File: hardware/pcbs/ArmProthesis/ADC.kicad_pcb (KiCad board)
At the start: 4 copper layers, 60.3 x 44.8 mm, 25 parts, among them J2 H_16_2.54mm, SW1 SW_Reed_SPDT, SW2 SW_Reed_SPDT, SW3 SW_Reed_SPDT, SW4 SW_Reed_SPDT, U1 AD7606BSTZ

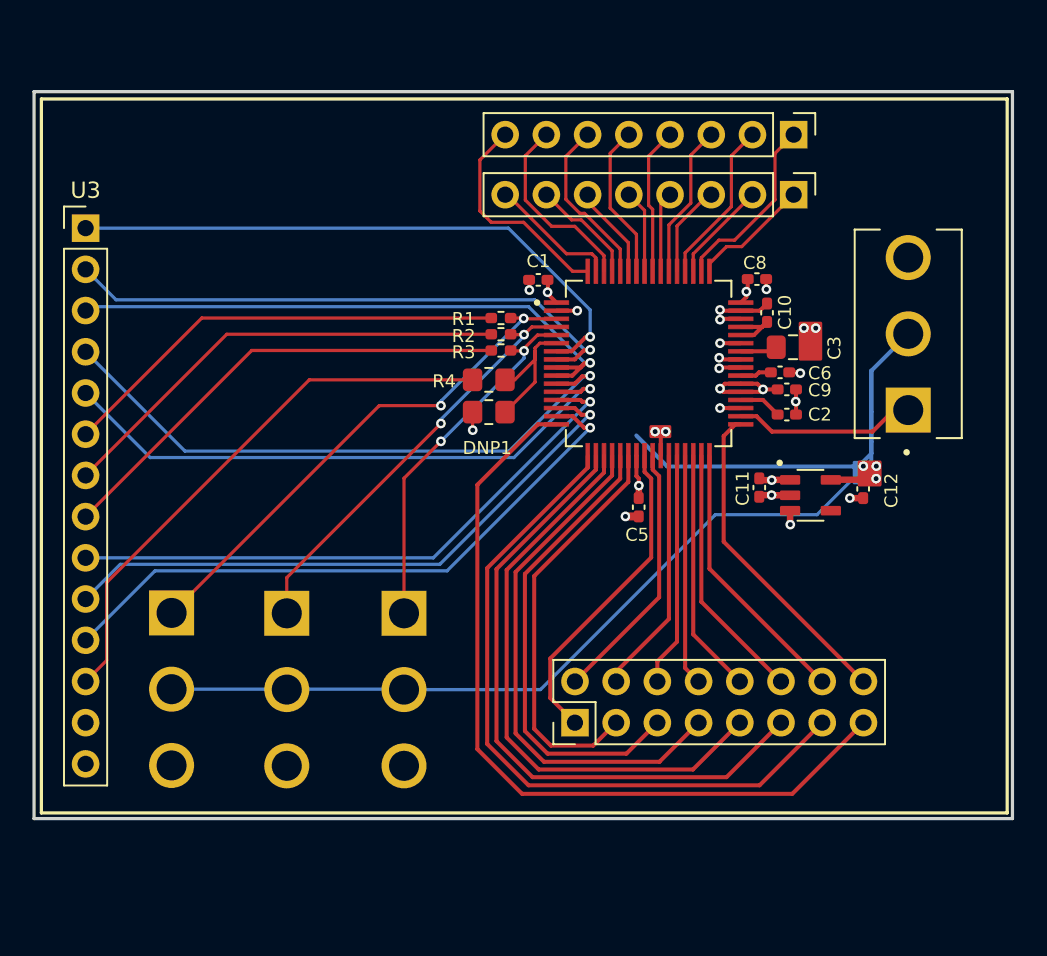
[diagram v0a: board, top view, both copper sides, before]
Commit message: ADC + sEMG changes
sEMG - connector updates
ADC - major changes - connectors, layout changes
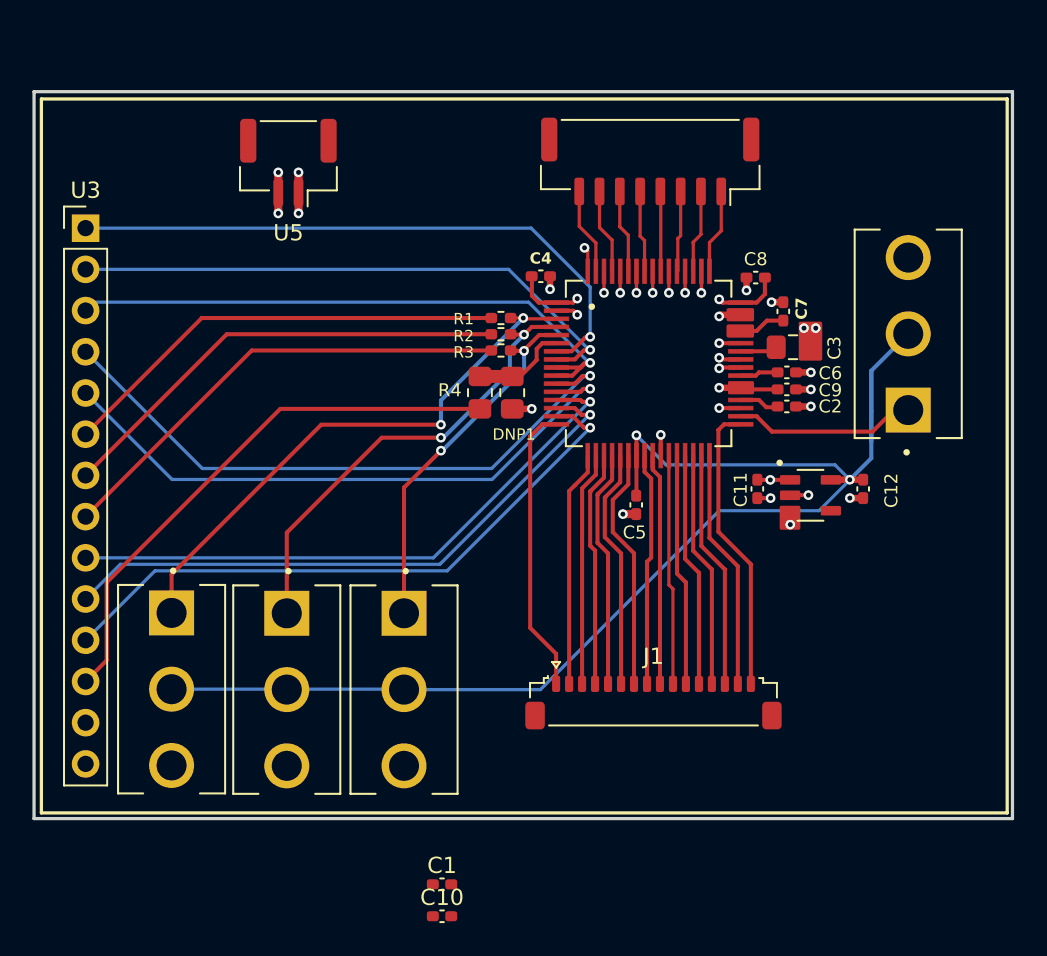
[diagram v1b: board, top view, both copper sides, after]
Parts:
- removed J2: H_16_2.54mm, Connector_PinHeader_2.54mm:PinHeader_2x08_P2.54mm_Vertical
- removed U4: ~, Connector_PinHeader_2.54mm:PinHeader_1x08_P2.54mm_Vertical
- added C4: 0.1uF, Capacitor_SMD:C_0402_1005Metric_Pad0.74x0.62mm_HandSolder, F.Cu at (170.3, 79.5)
- added C7: 1uF, Capacitor_SMD:C_0402_1005Metric_Pad0.74x0.62mm_HandSolder, F.Cu at (185.2, 81.7)
- added J1: H_16_2.54mm, Connector_JST:JST_SUR_SM16B-SURS-TF_1x16-1MP_P0.80mm_Horizontal, F.Cu at (177.2, 105.8)
- added U5: ~, Connector_JST:JST_GH_SM02B-GHS-TB_1x02-1MP_P1.25mm_Horizontal, F.Cu at (154.7, 72.5)
- SW1, SW2, SW3: moved to F.Cu
- U2: footprint Connector_PinHeader_2.54mm:PinHeader_1x08_P2.54mm_Vertical -> Connector_JST:JST_GH_SM08B-GHS-TB_1x08-1MP_P1.25mm_Horizontal
- moved C10 42.2 mm to (164.2, 119.0), turned to 0 degrees
- moved C1 37.7 mm to (164.2, 117.0)
- moved U2 9.07 mm to (177.0, 72.5), turned to 180 degrees
- moved DNP1 1.88 mm to (168.5, 86.7), turned to -90 degrees
- moved R4 0.96 mm to (166.5, 86.7), turned to 90 degrees
- moved C2 0.50 mm to (185.4, 87.5)
- moved C6 0.42 mm to (185.4, 85.5)
- moved C5 0.21 mm to (176.1, 93.6)
- moved C11 0.15 mm to (183.6, 92.6)
- moved C8 0.12 mm to (183.5, 79.6), turned to 0 degrees
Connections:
- net VDRIVE renamed +3.3V
- U1 pad 50: V1GND -> GND
- U1 pad 52: V2GND -> GND
- U1 pad 54: V3GND -> GND
- U1 pad 56: V4GND -> GND
- U1 pad 58: V5GND -> GND
- U1 pad 60: V6GND -> GND
- U1 pad 62: V7GND -> GND
- U1 pad 64: V8GND -> GND
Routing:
- net DB0: track 49.5 -> 17.8 mm
- net DB1: track 43.6 -> 14.5 mm
- net DB2: track 40.0 -> 14.4 mm
- net DB3: track 36.2 -> 14.5 mm
- net DB4: track 32.6 -> 14.7 mm
- net DB5: track 28.9 -> 14.9 mm
- net V8GND: track 13.5 -> 0.00 mm
- net GND: track 20.6 -> 32.4 mm, vias 19 -> 30
- net V7GND: track 11.8 -> 0.00 mm
- net V1GND: track 10.9 -> 0.00 mm
- net DB6: track 25.3 -> 15.0 mm
- net V6GND: track 10.1 -> 0.00 mm
- net V2GND: track 9.71 -> 0.00 mm
- net V5GND: track 9.14 -> 0.00 mm
- net V3GND: track 9.08 -> 0.00 mm
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
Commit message: BMS v0.3 + main folder reconstruction
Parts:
- removed C1: 0.1uF, Capacitor_SMD:C_0402_1005Metric_Pad0.74x0.62mm_HandSolder
- removed C10: 1uF, Capacitor_SMD:C_0402_1005Metric_Pad0.74x0.62mm_HandSolder
- added H1: MountingHole, MountingHole:MountingHole_2.7mm_M2.5, F.Cu at (147.5, 70.0)
- added H2: MountingHole, MountingHole:MountingHole_2.7mm_M2.5, F.Cu at (192.5, 70.0)
- added H3: MountingHole, MountingHole:MountingHole_2.7mm_M2.5, F.Cu at (192.5, 110.0)
- moved J1 6.80 mm to (177.2, 112.6)
- moved U5 6.41 mm to (160.0, 69.0)
- moved U2 3.60 mm to (177.0, 68.8)
- moved SW3 3.59 mm to (164.3, 107.6)
- moved SW1 3.59 mm to (150.0, 107.6)
- moved SW2 3.59 mm to (157.1, 107.6)
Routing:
- net DB0: track 17.8 -> 24.7 mm
- net DB8DOUTB: track 14.3 -> 21.1 mm
- net DB4: track 14.7 -> 21.5 mm
- net DB1: track 14.5 -> 21.3 mm
- net DB13: track 14.7 -> 21.5 mm
- net DB11: track 14.4 -> 21.2 mm
- net DB10: track 14.3 -> 21.1 mm
- net DB9: track 14.2 -> 21.0 mm
- net DB6: track 15.0 -> 21.8 mm
- net DB7/DOUTA: track 14.3 -> 21.1 mm
- net DB14: track 14.8 -> 21.6 mm
- net DB12: track 14.5 -> 21.3 mm
- net DB5: track 14.9 -> 21.7 mm
- net DB3: track 14.5 -> 21.3 mm
- net DB15: track 18.0 -> 24.8 mm
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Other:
- board size 60.3 x 44.8 mm -> 60.2 x 50.8 mm

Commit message: .
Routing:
- net GND: track 32.4 -> 31.6 mm
- net DB6: track 21.8 -> 21.2 mm
- net DB5: track 21.7 -> 21.1 mm
- net DB4: track 21.5 -> 21.0 mm
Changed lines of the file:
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@@
-	)
-	(segment
-		(start 176.13375 94.185)
-		(end 175.31625 94.185)
-		(width 0.5)
-		(layer "F.Cu")
-		(net 1)
 	)
 	(segment
@@
 	)
 	(via
-		(at 175.31625 94.185)
+		(at 176.13375 94.185)
 		(size 0.6)
 		(drill 0.3)
@@
 	(segment
 		(start 175.65 92.25)
-		(end 174.69025 93.20975)
-		(width 0.25)
-		(layer "F.Cu")
-		(net 19)
-	)
-	(segment
-		(start 174.69025 93.20975)
-		(end 174.69025 95.29025)
+		(end 175.45 92.45)
 		(width 0.25)
 		(layer "F.Cu")
@@
 	)
 	(segment
+		(start 175.45 92.45)
+		(end 175.45 96.05)
+		(width 0.25)
+		(layer "F.Cu")
+		(net 19)
+	)
+	(segment
+		(start 175.45 96.05)
+		(end 176 96.6)
+		(width 0.25)
+		(layer "F.Cu")
+		(net 19)
+	)
+	(segment
 		(start 175.65 90.58)
 		(end 175.65 92.25)
@@
 	)
 	(segment
-		(start 174.69025 95.29025)
-		(end 176 96.6)
-		(width 0.25)
-		(layer "F.Cu")
-		(net 19)
-	)
-	(segment
 		(start 181.2 89)
 		(end 181.2 95.275)
@@
 	)
 	(segment
-		(start 174.15 91.75)
-		(end 173.298 92.602)
-		(width 0.25)
-		(layer "F.Cu")
-		(net 30)
-	)
-	(segment
-		(start 173.298 92.602)
-		(end 173.298 96.13581)
-		(width 0.25)
-		(layer "F.Cu")
-		(net 30)
-	)
-	(segment
-		(start 173.6 96.43781)
-		(end 173.6 111.45)
-		(width 0.25)
-		(layer "F.Cu")
-		(net 30)
-	)
-	(segment
-		(start 173.298 96.13581)
-		(end 173.6 96.43781)
-		(width 0.25)
-		(layer "F.Cu")
-		(net 30)
-	)
-	(segment
 		(start 174.15 90.58)
 		(end 174.15 91.75)
@@
 	)
 	(segment
+		(start 173.6 92.3)
+		(end 173.6 111.45)
+		(width 0.25)
+		(layer "F.Cu")
+		(net 30)
+	)
+	(segment
+		(start 174.15 91.75)
+		(end 173.6 92.3)
+		(width 0.25)
+		(layer "F.Cu")
+		(net 30)
+	)
+	(segment
 		(start 176.65 77.325)
 		(end 176.375 77.05)
@@
 	)
 	(segment
-		(start 176.8 96.6)
+		(start 176.65 91.85)
+		(end 176.8 92)
+		(width 0.25)
+		(layer "F.Cu")
+		(net 33)
+	)
+	(segment
+		(start 176.8 92)
 		(end 176.8 111.45)
-		(width 0.25)
-		(layer "F.Cu")
-		(net 33)
-	)
-	(segment
-		(start 177.06 96.34)
-		(end 176.8 96.6)
 		(width 0.25)
 		(layer "F.Cu")
@@
 	)
 	(segment
-		(start 177.06 92.26)
-		(end 177.06 96.34)
-		(width 0.25)
-		(layer "F.Cu")
-		(net 33)
-	)
-	(segment
-		(start 176.65 91.85)
-		(end 177.06 92.26)
-		(width 0.25)
-		(layer "F.Cu")
-		(net 33)
-	)
-	(segment
 		(start 181.6 97.6)
 		(end 181.6 111.45)
@@
 	)
 	(segment
-		(start 173.749 95.949)
-		(end 174.4 96.6)
-		(width 0.25)
-		(layer "F.Cu")
-		(net 37)
-	)
-	(segment
-		(start 174.4 96.6)
-		(end 174.4 111.45)
-		(width 0.25)
-		(layer "F.Cu")
-		(net 37)
-	)
-	(segment
 		(start 174.65 91.95)
-		(end 173.749 92.851)
+		(end 174.4 92.2)
 		(width 0.25)
 		(layer "F.Cu")
@@
 	)
 	(segment
-		(start 173.749 92.851)
-		(end 173.749 95.949)
+		(start 174.4 92.2)
+		(end 174.4 111.45)
 		(width 0.25)
 		(layer "F.Cu")
@@
 	)
 	(segment
-		(start 175.15 92.1)
-		(end 174.2 93.05)
+		(start 174.95 92.3)
+		(end 174.95 96.35)
 		(width 0.25)
 		(layer "F.Cu")
@@
 	)
 	(segment
-		(start 174.2 93.05)
-		(end 174.2 95.6)
-		(width 0.25)
-		(layer "F.Cu")
-		(net 42)
-	)
-	(segment
-		(start 174.2 95.6)
-		(end 175.2 96.6)
+		(start 175.15 92.1)
+		(end 174.95 92.3)
 		(width 0.25)
 		(layer "F.Cu")
@@
 		(width 0.25)
 		(layer "F.Cu")
+		(net 42)
+	)
+	(segment
+		(start 174.95 96.35)
+		(end 175.2 96.6)
+		(width 0.25)
+		(layer "F.Cu")

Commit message: updates
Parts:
- removed DNP1: 10-47k, Resistor_SMD:R_0805_2012Metric_Pad1.20x1.40mm_HandSolder
- removed SW4: SW_Reed_SPDT, Switches:switch1
- removed U3: ~, Connector_PinHeader_2.54mm:PinHeader_1x14_P2.54mm_Vertical
- added J2: ~, Connector_PinHeader_2.54mm:PinHeader_1x12_P2.54mm_Vertical, F.Cu at (142.2, 79.1)
- added R5: 10k, Resistor_SMD:R_0603_1608Metric, F.Cu at (168.0, 85.4)
- C11, C12, C2, C4, C6, C8, C9: footprint Capacitor_SMD:C_0402_1005Metric_Pad0.74x0.62mm_HandSolder -> Capacitor_SMD:C_0402_1005Metric
- C3: footprint Capacitor_SMD:C_0805_2012Metric_Pad1.18x1.45mm_HandSolder -> Capacitor_SMD:C_0603_1608Metric
- C7: value 1uF -> 10 µF; footprint Capacitor_SMD:C_0402_1005Metric_Pad0.74x0.62mm_HandSolder -> Capacitor_SMD:C_0603_1608Metric
- R1, R2, R3: footprint Resistor_SMD:R_0402_1005Metric_Pad0.72x0.64mm_HandSolder -> Resistor_SMD:R_0402_1005Metric
- R4: value 1k -> 10k; footprint Resistor_SMD:R_0805_2012Metric_Pad1.20x1.40mm_HandSolder -> Resistor_SMD:R_0603_1608Metric
- moved H2 1.70 mm to (190.8, 70.0)
- moved H3 1.70 mm to (190.8, 110.0)
- moved R4 1.59 mm to (168.0, 87.2), turned to 180 degrees
- moved U5 0.80 mm to (160.0, 68.2)
- moved U2 0.80 mm to (177.0, 68.0)
- moved C2 0.05 mm to (185.4, 87.5)
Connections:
- R4 pad 1: SER/BYTE_SEL/PAR -> RST
- R4 pad 2: Net-(U1-SER/BYTE_SEL/~{PAR}) -> GND
- SW1 pad 1: Net-(U1-OS0) -> +3.3V
- SW1 pad 2: +3.3V -> Net-(U1-OS0)
- SW2 pad 1: Net-(U1-OS1) -> +3.3V
- SW2 pad 2: +3.3V -> Net-(U1-OS1)
- SW3 pad 1: Net-(U1-OS2) -> +3.3V
- SW3 pad 2: +3.3V -> Net-(U1-OS2)
- U1 pad 34: Net-(U1-REF_SELECT) -> +3.3V
- U1 pad 6: Net-(U1-SER/BYTE_SEL/~{PAR}) -> GND
- U1 pad 8: RANGE -> GND
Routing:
- net RANGE: track 35.2 -> 0.00 mm, vias 1 -> 0
- net SER/BYTE_SEL/PAR: track 34.1 -> 0.00 mm
- net Net-(U1-REF_SELECT): track 12.9 -> 0.00 mm
- net GND: track 31.6 -> 40.7 mm, vias 30 -> 33
- net +3.3V: track 86.3 -> 77.5 mm
- net Net-(U1-OS2): track 24.7 -> 31.0 mm
- net Net-(U1-SER/BYTE_SEL/~{PAR}): track 5.47 -> 0.00 mm
- net Net-(U1-OS0): track 35.9 -> 40.6 mm
- net STBY: track 36.0 -> 39.8 mm
- net Net-(U1-OS1): track 30.2 -> 33.3 mm
- net RST: track 38.7 -> 41.7 mm
- net V6: track 8.74 -> 9.56 mm
- net V8: track 8.94 -> 9.76 mm
- net V7: track 8.84 -> 9.66 mm
- net V5: track 8.63 -> 9.45 mm
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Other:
- board size 60.2 x 50.8 mm -> 56.7 x 50.8 mm

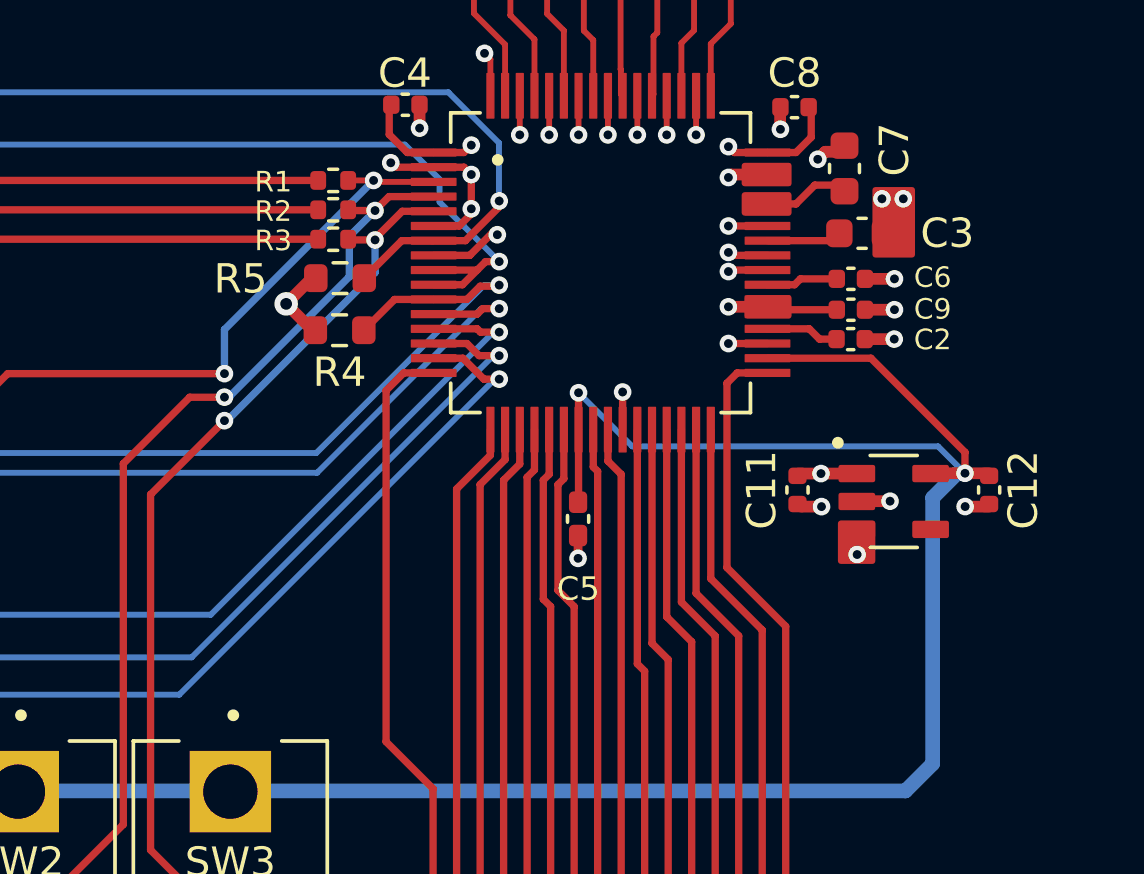
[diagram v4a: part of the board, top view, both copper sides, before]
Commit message: Fixed compatibility of connectors  + new BMS chip
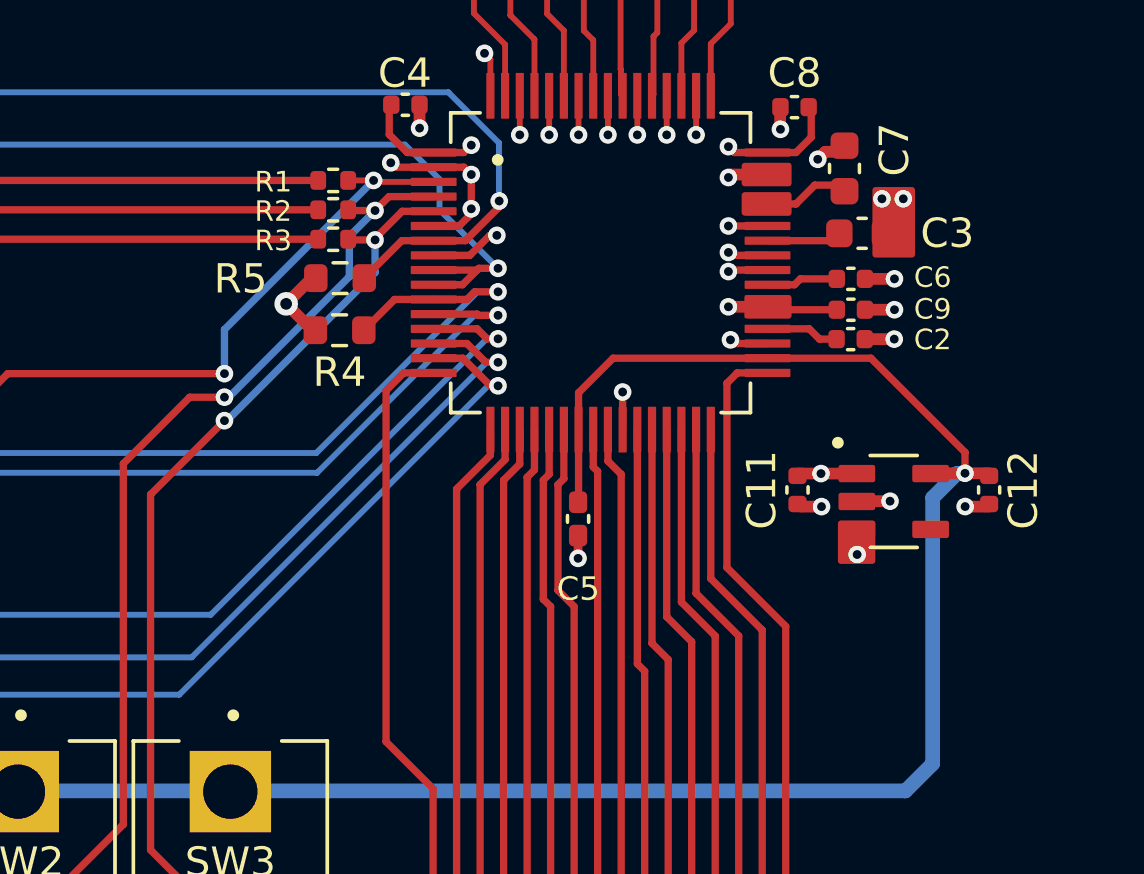
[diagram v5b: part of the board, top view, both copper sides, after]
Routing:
- net +3.3V: track 77.5 -> 70.2 mm, vias 2 -> 1

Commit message: Ordered versions
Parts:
- removed J1: H_16_2.54mm, Connector_JST:JST_SUR_SM16B-SURS-TF_1x16-1MP_P0.80mm_Horizontal
- added U3: ~, Connector_JST:JST_SH_SM08B-SRSS-TB_1x08-1MP_P1.00mm_Horizontal, F.Cu at (183.7, 101.8)
- added U4: ~, Connector_JST:JST_SH_SM08B-SRSS-TB_1x08-1MP_P1.00mm_Horizontal, F.Cu at (171.8, 101.8)
- SW1, SW2, SW3: footprint Switches:switch1 -> Button_Switch_SMD:SW_SPDT_Shouhan_MSK12C02
- moved H3 10.7 mm to (192.9, 99.5)
- moved SW1 9.35 mm to (147.6, 98.5)
- moved SW3 9.35 mm to (162.0, 98.5)
- moved SW2 9.35 mm to (154.7, 98.5)
- moved J2 4.67 mm to (142.2, 74.4)
- moved U2 3.42 mm to (177.0, 71.5)
- moved U5 3.42 mm to (160.0, 71.6)
- moved H2 3.16 mm to (192.9, 72.4)
- moved H1 3.05 mm to (149.4, 72.4)
- moved C5 0.34 mm to (175.8, 93.8)
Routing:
- net DB0: track 24.7 -> 13.0 mm
- net DB6: track 21.2 -> 9.77 mm
- net DB7/DOUTA: track 20.9 -> 9.77 mm
- net DB5: track 21.1 -> 9.98 mm
- net DB4: track 21.0 -> 10.2 mm
- net DB3: track 21.1 -> 10.4 mm
- net DB2: track 21.2 -> 10.6 mm
- net DB8DOUTB: track 21.1 -> 10.5 mm
- net DB1: track 21.3 -> 10.8 mm
- net DB9: track 21.0 -> 10.5 mm
- net DB10: track 21.1 -> 10.7 mm
- net DB11: track 21.2 -> 10.9 mm
- net DB12: track 21.3 -> 11.1 mm
- net DB13: track 21.5 -> 11.3 mm
- net DB14: track 21.6 -> 11.5 mm
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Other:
- board size 56.7 x 50.8 mm -> 57.7 x 37.6 mm

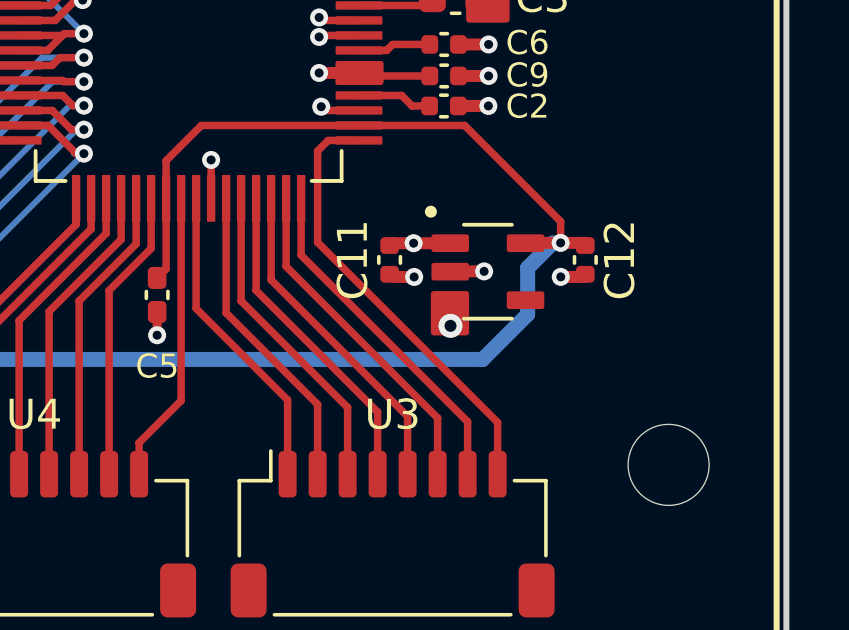
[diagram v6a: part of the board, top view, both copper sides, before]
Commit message: Synced the files with the latest versions
The files that were merged were one version behind. Also the names of the projects were renamed for clarity.
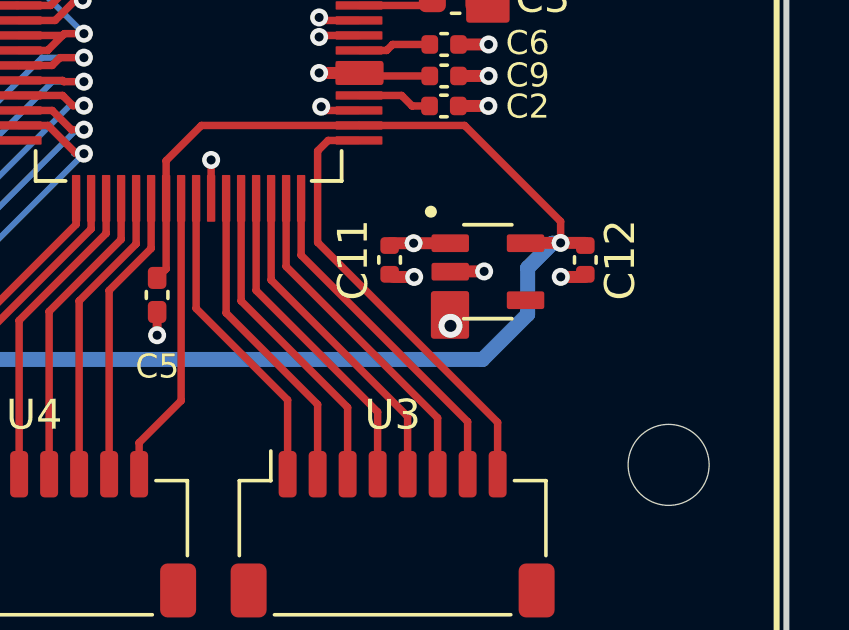
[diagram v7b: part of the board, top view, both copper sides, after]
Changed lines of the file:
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@@
 	(gr_rect
 		(start 185.075 93.775)
-		(end 186.15 95.05)
+		(end 186.15 95.161445)
 		(stroke
 			(width 0.2)
